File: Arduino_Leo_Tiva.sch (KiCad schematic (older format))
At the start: 51 parts, among them J1 USB_OTG, J10 Digital, J11 TDI, J12 TDO, J13 TXD, J14 RXD, J15 -AREF, J16 +AREF, J17 SPI 2 (D6,D7), J18 SERIAL 3, 4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

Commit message: Added as-built Mfg. part numbers and full descriptions to each component.
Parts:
- C1: Description (none) -> 24pF ±5% 50V Ceramic Capacitor C0G, NP0 0603; Part # (none) -> CC0603JRNPO9BN240
- C10, C16, C8: Description (none) -> 6.3 V to 25 V, X5R/X7R ceramic chip; Part # (none) -> CL21A226MOCLRNC; Type 6.3 V to 25 V, X5R/X7R ceramic chip -> (none)
- C15, C7, C9: Description (none) -> 6.3 V to 25 V, X5R/X7R ceramic chip; Part # (none) -> CC0603JRX7R8BB104; Type 6.3 V to 25 V, X5R/X7R ceramic chip -> (none)
- C17: Description (none) -> 22µF ±10% Molded Tantalum Capacitors 16V 2413 (6032 Metric)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; Part # (none) -> T491C226K016AT; Type Tantalum -> (none)
- C3: Description (none) -> 24pF ±5% 50V Ceramic Capacitor C0G, NP0 0603; Part # (none) -> C0603C100J5GACTU
- C4: Description (none) -> CAP CER 10PF 50V C0G/NP0 0603; Part # (none) -> C0603C100J5GACTU
- C5, C6: Description (none) -> 6.3 V to 25 V, X5R/X7R ceramic chip; Type 6.3 V to 25 V, X5R/X7R ceramic chip -> (none)
- D1: Description LED GREEN DIFFUSED 0805 SMD -> Green 570nm LED Indication - Discrete 2.2V 0805 (2012 Metri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; Vf 2.2V -> (none)
- J1: Description (none) -> USB - micro B USB 2.0 Receptacle Connector 5 Position Surfa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
- R1: Description (none) -> 10k Ohm ±1% 0.1W, 1/10W Chip Resistor 0603 (1608 Metric) Au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; Part # (none) -> ERJ-3EKF1002V
- R2: Description (none) -> 1M Ohm ±1% 0.1W, 1/10W Chip Resistor 0603 (1608 Metric) Aut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; Part # (none) -> ERJ-3EKF1004V
- R3: Description (none) -> 75 Ohm ±1% 0.1W, 1/10W Chip Resistor 0603 (1608 Metric) Aut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; Part # (none) -> ERJ-3EKF75R0V
- R4: Description (none) -> 100 Ohm ±1% 0.1W, 1/10W Chip Resistor 0603 (1608 Metric) Au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; Part # (none) -> ERJ-3EKF1000V
- U1: Description (none) -> ARM® Cortex®-M4F Tiva™ C Microcontroller IC 32-Bit 80MHz 25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; Part # (none) -> TM4C123GH6PMI7
- U2: Description (none) -> Linear Voltage Regulator IC Positive Fixed Output 3.3V 800m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; Part # (none) -> LM1117IMPX-3.3/NOPB
- Y1: Description (none) -> 32.768kHz ±5ppm Crystal 12.5pF 35 kOhm -20°C ~ 70°C Through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
- Y2: Description (none) -> 16MHz ±20ppm Crystal 8pF 50 Ohm -10°C ~ 70°C Surface Mount 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
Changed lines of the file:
@@
 Sheet 1 1
 Title "Arduino-Tiva-TM4C123G"
-Date ""
-Rev "v0.1"
-Comp ""
+Date "2017-04-17"
+Rev "v1.0"
+Comp "Jacob Miller"
 Comment1 ""
 Comment2 ""
@@
 F 1 "TM4C123GH6PM" H 6100 5300 50  0000 L CNN
 F 2 "Housings_QFP:LQFP-64_10x10mm_Pitch0.5mm" H 5450 3300 50  0001 C CIN
-F 3 "" H 5450 3500 50  0001 C CNN
+F 3 "http://www.ti.com/lit/ds/symlink/tm4c123gh6pm.pdf" H 5450 3500 50  0001 C CNN
+F 4 "ARM® Cortex®-M4F Tiva™ C Microcontroller IC 32-Bit 80MHz 256KB (256K x 8) FLASH 64-LQFP (10x10)" H 5450 3300 60  0001 C CNN "Description"
+F 5 "TM4C123GH6PMI7" H 5450 3300 60  0001 C CNN "Part #"
 	1    5450 3300
 	1    0    0    -1
@@
 F 1 "10k" V 1500 2650 50  0000 C CNN
 F 2 "Resistors_SMD:R_0603" V 1430 2650 50  0001 C CNN
-F 3 "" H 1500 2650 50  0001 C CNN
+F 3 "http://industrial.panasonic.com/www-cgi/jvcr13pz.cgi?E+PZ+3+AOA0002+ERJ3EKF1002V+7+WW" H 1500 2650 50  0001 C CNN
+F 4 "10k Ohm ±1% 0.1W, 1/10W Chip Resistor 0603 (1608 Metric) Automotive AEC-Q200 Thick Film" V 1500 2650 60  0001 C CNN "Description"
+F 5 "ERJ-3EKF1002V" V 1500 2650 60  0001 C CNN "Part #"
 	1    1500 2650
 	1    0    0    -1
@@
 F 3 "http://cfd.citizen.co.jp/english/prod-tech/product/pdf/datasheet_TF/CFS-145%20CFS-206%20CFV-206_E.pdf" H 2750 4950 50  0001 C CNN
 F 4 "CFS-20632768HZFB" H 2750 4950 60  0001 C CNN "Part #"
+F 5 "32.768kHz ±5ppm Crystal 12.5pF 35 kOhm -20°C ~ 70°C Through Hole Cylindrical Can, Radial" H 2750 4950 60  0001 C CNN "Description"
 	1    2750 4950
 	1    0    0    -1
@@
 F 1 "24pF" H 2410 4570 50  0000 L CNN
 F 2 "Capacitors_SMD:C_0603" H 2400 4650 50  0001 C CNN
-F 3 "" H 2400 4650 50  0001 C CNN
+F 3 "http://www.yageo.com/documents/recent/UPY-GP_NP0_16V-to-50V_16.pdf" H 2400 4650 50  0001 C CNN
+F 4 "24pF ±5% 50V Ceramic Capacitor C0G, NP0 0603" H 2400 4650 60  0001 C CNN "Description"
+F 5 "CC0603JRNPO9BN240" H 2400 4650 60  0001 C CNN "Part #"
 	1    2400 4650
 	0    -1   -1   0
@@
 F 1 "10pF" H 3110 3570 50  0000 L CNN
 F 2 "Capacitors_SMD:C_0603" H 3100 3650 50  0001 C CNN
-F 3 "" H 3100 3650 50  0001 C CNN
+F 3 "https://www.digikey.com/catalog/en/partgroup/c0g-np0-dielectric-commercial-grade/3830?mpart=C0603C100J5GACTU&vendor=399" H 3100 3650 50  0001 C CNN
+F 4 "CAP CER 10PF 50V C0G/NP0 0603" H 3100 3650 60  0001 C CNN "Description"
+F 5 "C0603C100J5GACTU" H 3100 3650 60  0001 C CNN "Part #"
 	1    3100 3650
 	1    0    0    -1
@@
 F 1 "10pF" H 2410 3570 50  0000 L CNN
 F 2 "Capacitors_SMD:C_0603" H 2400 3650 50  0001 C CNN
-F 3 "" H 2400 3650 50  0001 C CNN
+F 3 "https://www.digikey.com/catalog/en/partgroup/c0g-np0-dielectric-commercial-grade/3830?mpart=C0603C100J5GACTU&vendor=399" H 2400 3650 50  0001 C CNN
+F 4 "24pF ±5% 50V Ceramic Capacitor C0G, NP0 0603" H 2400 3650 60  0001 C CNN "Description"
+F 5 "C0603C100J5GACTU" H 2400 3650 60  0001 C CNN "Part #"
 	1    2400 3650
 	1    0    0    -1
@@
 F 3 "http://www.ndk.com/images/products/catalog/c_NX5032GA_e.pdf" H 2750 3450 50  0001 C CNN
 F 4 "NX5032GA-16MHZ-STD-CSK-4" H 2750 3450 60  0001 C CNN "Part #"
+F 5 "16MHz ±20ppm Crystal 8pF 50 Ohm -10°C ~ 70°C Surface Mount 2-SMD, No Lead" H 2750 3450 60  0001 C CNN "Description"
 	1    2750 3450
 	1    0    0    -1
@@
 F 2 "Capacitors_SMD:C_0603" H 8200 1100 50  0001 C CNN
 F 3 "http://www.yageo.com/documents/recent/UPY-GPHC_X7R_6.3V-to-50V_17.pdf" H 8200 1100 50  0001 C CNN
-F 4 "6.3 V to 25 V, X5R/X7R ceramic chip" H 8200 1100 60  0001 C CNN "Type"
+F 4 "6.3 V to 25 V, X5R/X7R ceramic chip" H 8200 1100 60  0001 C CNN "Description"
 F 5 "CC0603JRX7R8BB104" H 8200 1100 60  0001 C CNN "Part #"
 	1    8200 1100
@@
 F 2 "Capacitors_SMD:C_0805" H 8500 1100 50  0001 C CNN
 F 3 "http://www.samsungsem.com/kr/support/library/product-catalog/__icsFiles/afieldfile/2016/09/27/MLCC.pdf" H 8500 1100 50  0001 C CNN
-F 4 "6.3 V to 25 V, X5R/X7R ceramic chip" H 8500 1100 60  0001 C CNN "Type"
+F 4 "6.3 V to 25 V, X5R/X7R ceramic chip" H 8500 1100 60  0001 C CNN "Description"
 F 5 "CL21A226MOCLRNC" H 8500 1100 60  0001 C CNN "Part #"
 	1    8500 1100
@@
 F 2 "Capacitors_SMD:C_0805" H 9100 1100 50  0001 C CNN
 F 3 "" H 9100 1100 50  0001 C CNN
-F 4 "6.3 V to 25 V, X5R/X7R ceramic chip" H 9100 1100 60  0001 C CNN "Type"
+F 4 "6.3 V to 25 V, X5R/X7R ceramic chip" H 9100 1100 60  0001 C CNN "Description"
+F 5 "CL21A226MOCLRNC" H 9100 1100 60  0001 C CNN "Part #"
 	1    9100 1100
 	1    0    0    -1
@@
 F 2 "Capacitors_SMD:C_0805" H 9700 1100 50  0001 C CNN
 F 3 "" H 9700 1100 50  0001 C CNN
-F 4 "6.3 V to 25 V, X5R/X7R ceramic chip" H 9700 1100 60  0001 C CNN "Type"
+F 4 "6.3 V to 25 V, X5R/X7R ceramic chip" H 9700 1100 60  0001 C CNN "Description"
+F 5 "CL21A226MOCLRNC" H 9700 1100 60  0001 C CNN "Part #"
 	1    9700 1100
 	1    0    0    -1
@@
 F 1 "1M" V 10450 4150 50  0000 C CNN
 F 2 "Resistors_SMD:R_0603" V 10380 4150 50  0001 C CNN
-F 3 "" H 10450 4150 50  0001 C CNN
+F 3 "https://industrial.panasonic.com/cdbs/www-data/pdf/RDA0000/AOA0000C283.pdf" H 10450 4150 50  0001 C CNN
+F 4 "1M Ohm ±1% 0.1W, 1/10W Chip Resistor 0603 (1608 Metric) Automotive AEC-Q200 Thick Film" V 10450 4150 60  0001 C CNN "Description"
+F 5 "ERJ-3EKF1004V" V 10450 4150 60  0001 C CNN "Part #"
 	1    10450 4150
 	0    1    1    0
@@
 F 2 "TO_SOT_Packages_SMD_Local:SOT-223-3Lead_TabPin2" H 2000 1300 50  0001 C CIN
 F 3 "http://www.ti.com/lit/ds/symlink/lm1117.pdf" H 2000 1200 50  0001 C CNN
+F 4 "Linear Voltage Regulator IC Positive Fixed Output 3.3V 800mA SOT-223-4" H 2000 1200 60  0001 C CNN "Description"
+F 5 "LM1117IMPX-3.3/NOPB" H 2000 1200 60  0001 C CNN "Part #"
 	1    2000 1200
 	1    0    0    -1
@@
 F 1 "75" V 2550 1400 50  0000 C CNN
 F 2 "Resistors_SMD:R_0603" V 2480 1400 50  0001 C CNN
-F 3 "" H 2550 1400 50  0001 C CNN
+F 3 "http://industrial.panasonic.com/www-cgi/jvcr13pz.cgi?E+PZ+3+AOA0002+ERJ3EKF75R0V+7+WW" H 2550 1400 50  0001 C CNN
+F 4 "75 Ohm ±1% 0.1W, 1/10W Chip Resistor 0603 (1608 Metric) Automotive AEC-Q200 Thick Film" V 2550 1400 60  0001 C CNN "Description"
+F 5 "ERJ-3EKF75R0V" V 2550 1400 60  0001 C CNN "Part #"
 	1    2550 1400
 	1    0    0    -1
@@
 F 2 "LEDs:LED_0805" H 2550 1800 50  0001 C CNN
 F 3 "http://www.osram-os.com/Graphics/XPic9/00078860_0.pdf" H 2550 1800 50  0001 C CNN
-F 4 "2.2V" H 2550 1800 60  0001 C CNN "Vf"
-F 5 "20mA" H 2550 1800 60  0001 C CNN "Current "
-F 6 "LED GREEN DIFFUSED 0805 SMD" H 2550 1800 60  0001 C CNN "Description"
-F 7 "LG R971-KN-1" H 2550 1800 60  0001 C CNN "Part #"
+F 4 "20mA" H 2550 1800 60  0001 C CNN "Current "
+F 5 "Green 570nm LED Indication - Discrete 2.2V 0805 (2012 Metric)" H 2550 1800 60  0001 C CNN "Description"
+F 6 "LG R971-KN-1" H 2550 1800 60  0001 C CNN "Part #"
 	1    2550 1800
 	0    -1   -1   0
@@
 F 2 "Capacitors_SMD:C_0603" H 8800 1100 50  0001 C CNN
 F 3 "" H 8800 1100 50  0001 C CNN
-F 4 "6.3 V to 25 V, X5R/X7R ceramic chip" H 8800 1100 60  0001 C CNN "Type"
+F 4 "6.3 V to 25 V, X5R/X7R ceramic chip" H 8800 1100 60  0001 C CNN "Description"
+F 5 "CC0603JRX7R8BB104" H 8800 1100 60  0001 C CNN "Part #"
 	1    8800 1100
 	1    0    0    -1
@@
 F 2 "Capacitors_SMD:C_0603" H 9400 1100 50  0001 C CNN
 F 3 "" H 9400 1100 50  0001 C CNN
-F 4 "6.3 V to 25 V, X5R/X7R ceramic chip" H 9400 1100 60  0001 C CNN "Type"
+F 4 "6.3 V to 25 V, X5R/X7R ceramic chip" H 9400 1100 60  0001 C CNN "Description"
+F 5 "CC0603JRX7R8BB104" H 9400 1100 60  0001 C CNN "Part #"
 	1    9400 1100
 	1    0    0    -1
@@
 F 4 "10118192-0001LF" H 9200 5450 60  0001 C CNN "Part #"
 F 5 "http://portal.fciconnect.com/Comergent//fci/drawing/10118192.pdf" H 9200 5450 60  0001 C CNN "Drawing"
+F 6 "USB - micro B USB 2.0 Receptacle Connector 5 Position Surface Mount, Right Angle" H 9200 5450 60  0001 C CNN "Description"
 	1    9200 5450
 	1    0    0    -1
@@
 F 2 "Capacitors_SMD:C_0805" H 10300 1100 50  0001 C CNN
 F 3 "" H 10300 1100 50  0001 C CNN
-F 4 "6.3 V to 25 V, X5R/X7R ceramic chip" H 10300 1100 60  0001 C CNN "Type"
+F 4 "6.3 V to 25 V, X5R/X7R ceramic chip" H 10300 1100 60  0001 C CNN "Description"
+F 5 "CL21A226MOCLRNC" H 10300 1100 60  0001 C CNN "Part #"
 	1    10300 1100
 	1    0    0    -1
@@
 F 2 "Capacitors_SMD:C_0603" H 10000 1100 50  0001 C CNN
 F 3 "" H 10000 1100 50  0001 C CNN
-F 4 "6.3 V to 25 V, X5R/X7R ceramic chip" H 10000 1100 60  0001 C CNN "Type"
+F 4 "6.3 V to 25 V, X5R/X7R ceramic chip" H 10000 1100 60  0001 C CNN "Description"
+F 5 "CC0603JRX7R8BB104" H 10000 1100 60  0001 C CNN "Part #"
 	1    10000 1100
 	1    0    0    -1
@@
 F 1 "100" V 1200 2900 50  0000 C CNN
 F 2 "Resistors_SMD:R_0603" V 1130 2900 50  0001 C CNN
-F 3 "" H 1200 2900 50  0001 C CNN
+F 3 "https://industrial.panasonic.com/cdbs/www-data/pdf/RDA0000/AOA0000C283.pdf" H 1200 2900 50  0001 C CNN
+F 4 "100 Ohm ±1% 0.1W, 1/10W Chip Resistor 0603 (1608 Metric) Automotive AEC-Q200 Thick Film" V 1200 2900 60  0001 C CNN "Description"
+F 5 "ERJ-3EKF1000V" V 1200 2900 60  0001 C CNN "Part #"
 	1    1200 2900
 	0    1    1    0
@@
 F 1 "22.0uF" H 2925 1300 50  0000 L CNN
 F 2 "Capacitors_Tantalum_SMD:CP_Tantalum_Case-C_EIA-6032-28_Hand" H 2938 1250 50  0001 C CNN
-F 3 "" H 2900 1400 50  0001 C CNN
-F 4 "Tantalum" H 2900 1400 60  0001 C CNN "Type"
+F 3 "http://www.kemet.com/Lists/ProductCatalog/Attachments/254/KEM_T2005_T491.pdf" H 2900 1400 50  0001 C CNN
+F 4 "22µF ±10% Molded Tantalum Capacitors 16V 2413 (6032 Metric) 1.6 Ohm" H 2900 1400 60  0001 C CNN "Description"
+F 5 "T491C226K016AT" H 2900 1400 60  0001 C CNN "Part #"
 	1    2900 1400
 	1    0    0    -1

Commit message: Fixed issue with incorrect schematic symbol and footprint for 3.3V regulator IC. Fixed typo in path
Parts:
- removed U2: LM1117IMPX-3.3, TO_SOT_Packages_SMD_Local:SOT-223-3Lead_TabPin2, symbol LT1129CST-3.3
- added U2: LM1117-3.3, TO_SOT_Packages_SMD_Local:SOT-223, symbol LM1117-3.3
- C3: Description 24pF ±5% 50V Ceramic Capacitor C0G, NP0 0603 -> CAP CER 10PF 50V C0G/NP0 0603
- J3: value RST -> ~RST
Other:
- note added: "1 - Vin\n2 - Gnd\n3 - Vout"
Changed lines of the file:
@@
 P 1850 2650
 F 0 "J3" H 1850 2800 60  0000 C CNN
-F 1 "RST" H 1850 2500 60  0000 C CNN
+F 1 "~RST" H 1850 2500 60  0000 C CNN
 F 2 "Pin_Headers:Pin_Header_Straight_1x01_Pitch2.54mm" H 1850 2650 60  0001 C CNN
 F 3 "" H 1850 2650 60  0000 C CNN
@@
 F 2 "Capacitors_SMD:C_0603" H 2400 3650 50  0001 C CNN
 F 3 "https://www.digikey.com/catalog/en/partgroup/c0g-np0-dielectric-commercial-grade/3830?mpart=C0603C100J5GACTU&vendor=399" H 2400 3650 50  0001 C CNN
-F 4 "24pF ±5% 50V Ceramic Capacitor C0G, NP0 0603" H 2400 3650 60  0001 C CNN "Description"
+F 4 "CAP CER 10PF 50V C0G/NP0 0603" H 2400 3650 60  0001 C CNN "Description"
 F 5 "C0603C100J5GACTU" H 2400 3650 60  0001 C CNN "Part #"
 	1    2400 3650
@@
 F 3 "" H 10700 4050 50  0001 C CNN
 	1    10700 4050
-	1    0    0    -1
-$EndComp
-$Comp
-L LT1129CST-3.3 U2
-U 1 1 58E05D8A
-P 2000 1200
-F 0 "U2" H 1750 1400 50  0000 C CNN
-F 1 "LM1117IMPX-3.3" H 2150 1400 50  0000 C CNN
-F 2 "TO_SOT_Packages_SMD_Local:SOT-223-3Lead_TabPin2" H 2000 1300 50  0001 C CIN
-F 3 "http://www.ti.com/lit/ds/symlink/lm1117.pdf" H 2000 1200 50  0001 C CNN
-F 4 "Linear Voltage Regulator IC Positive Fixed Output 3.3V 800mA SOT-223-4" H 2000 1200 60  0001 C CNN "Description"
-F 5 "LM1117IMPX-3.3/NOPB" H 2000 1200 60  0001 C CNN "Part #"
-	1    2000 1200
 	1    0    0    -1
 $EndComp
@@
 	2550 1550 2550 1650
 Wire Wire Line
-	2450 1150 2900 1150
+	2300 1150 2900 1150
 Connection ~ 2550 1150
 Wire Wire Line
-	2000 1500 2000 1650
+	2000 1450 2000 1650
 Wire Wire Line
 	2550 1950 2550 2100
@@
 	1250 950  1250 1300
 Wire Wire Line
-	1100 1150 1550 1150
+	1100 1150 1700 1150
 Connection ~ 1250 1150
 Wire Wire Line
@@
 Wire Wire Line
 	9100 5900 9200 5900
+$Comp
+L LM1117-3.3 U2
+U 1 1 5908BBBE
+P 2000 1150
+F 0 "U2" H 2100 900 50  0000 C CNN
+F 1 "LM1117-3.3" H 2000 1400 50  0000 C CNN
+F 2 "TO_SOT_Packages_SMD_Local:SOT-223" H 2000 1150 50  0001 C CNN
+F 3 "http://www.ti.com/lit/ds/symlink/lm1117.pdf" H 2000 1150 50  0001 C CNN
+F 4 "Linear Voltage Regulator IC Positive Fixed Output 3.3V 800mA SOT-223-4" H 2000 1150 60  0001 C CNN "Description"
+	1    2000 1150
+	1    0    0    -1
+$EndComp
+Text Notes 1800 800  0    60   ~ 0
+1 - Vin\n2 - Gnd\n3 - Vout
 $EndSCHEMATC

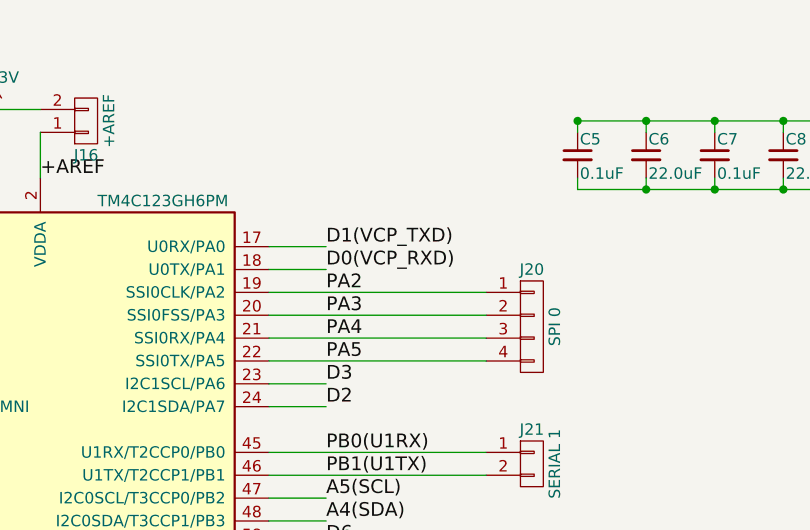
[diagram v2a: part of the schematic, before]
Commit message: Fixed "Swap UART Labels on D0,D1 #7"
Had U0Tx and U0Rx labled incorrectly in schematic.
Fixed labels and rerouted signals to correct pins.
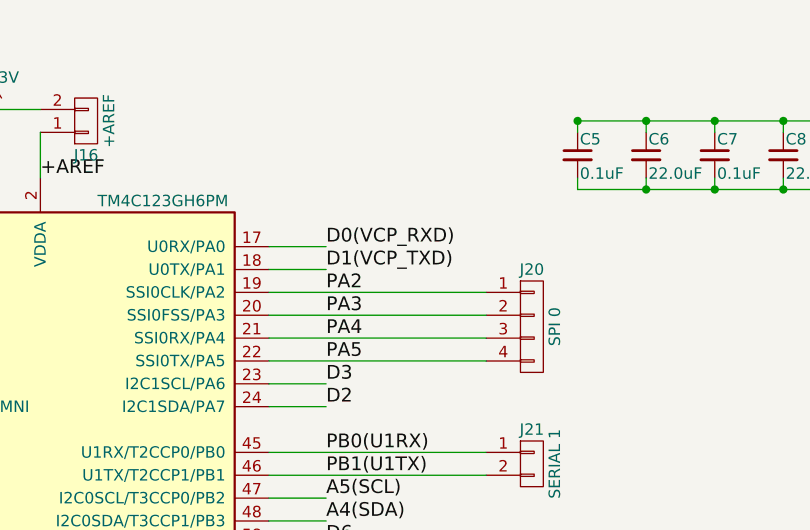
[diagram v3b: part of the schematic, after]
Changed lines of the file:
@@
 Text Label 3800 1500 2    60   ~ 0
 A3
+Text Label 7100 1600 0    60   ~ 0
+D1(VCP_TXD)
 Text Label 7100 1500 0    60   ~ 0
-D1(VCP_TXD)
-Text Label 7100 1600 0    60   ~ 0
 D0(VCP_RXD)
 Text Label 7100 3300 0    60   ~ 0

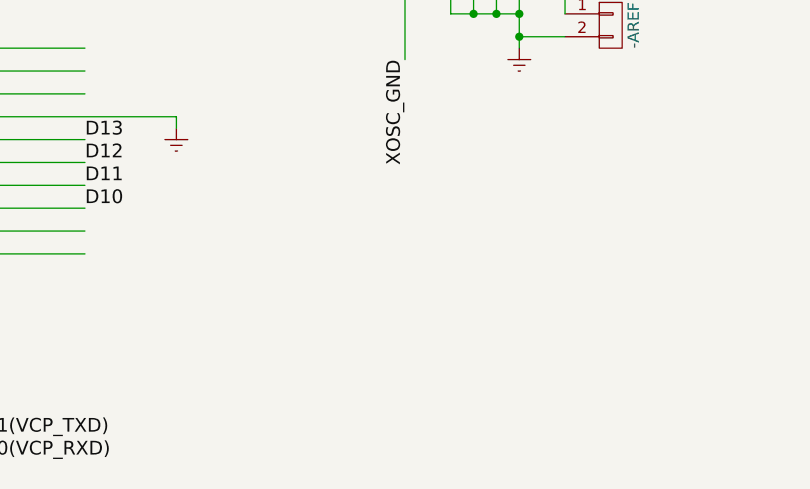
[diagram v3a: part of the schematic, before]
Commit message: Modified LEGO mounting hole - Increased width by 0.05 mm - Removed through hole plating (now NPTH)
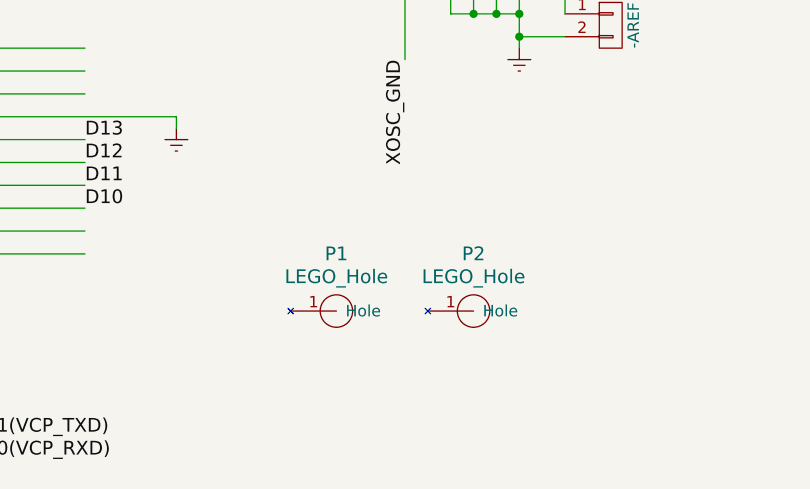
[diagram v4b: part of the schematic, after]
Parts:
- added P1, P2: LEGO_Hole, Custom-Mounting-Holes:Lego-Hole, symbol LEGO_Hole
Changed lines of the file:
@@
 LIBS:embedded-microcontrollers
 LIBS:myParts
-LIBS:Arduino_As_Uno-cache
 LIBS:Arduino_Leo_Tiva-cache
 EELAYER 25 0
@@
 Text Notes 1800 800  0    60   ~ 0
 1 - Vin\n2 - Gnd\n3 - Vout
+$Comp
+L LEGO_Hole P1
+U 1 1 5911A175
+P 4750 6850
+F 0 "P1" H 4750 7100 60  0000 C CNN
+F 1 "LEGO_Hole" H 4750 7000 60  0000 C CNN
+F 2 "Custom-Mounting-Holes:Lego-Hole" H 4750 6850 60  0001 C CNN
+F 3 "" H 4750 6850 60  0001 C CNN
+	1    4750 6850
+	1    0    0    -1
+$EndComp
+$Comp
+L LEGO_Hole P2
+U 1 1 5911A212
+P 5350 6850
+F 0 "P2" H 5350 7100 60  0000 C CNN
+F 1 "LEGO_Hole" H 5350 7000 60  0000 C CNN
+F 2 "Custom-Mounting-Holes:Lego-Hole" H 5350 6850 60  0001 C CNN
+F 3 "" H 5350 6850 60  0001 C CNN
+	1    5350 6850
+	1    0    0    -1
+$EndComp
 $EndSCHEMATC
